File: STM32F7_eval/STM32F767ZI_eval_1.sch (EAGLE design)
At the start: 100 parts, among them CN3 GROVE-4P-CONN-I2C-90D, CN4 GROVE-4P-CONN-AN01-90D, CN5 ARDUINO_COMPAT_IF, CN6 STLINKV21_SWD_IF, CN7 WFT0750CZ09-SMD_, CN8 MCO_IF, CN9 UART_IF, Q1 PMF370XN_, SW1 SKRPACE010_, SW2 SKRPACE010_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

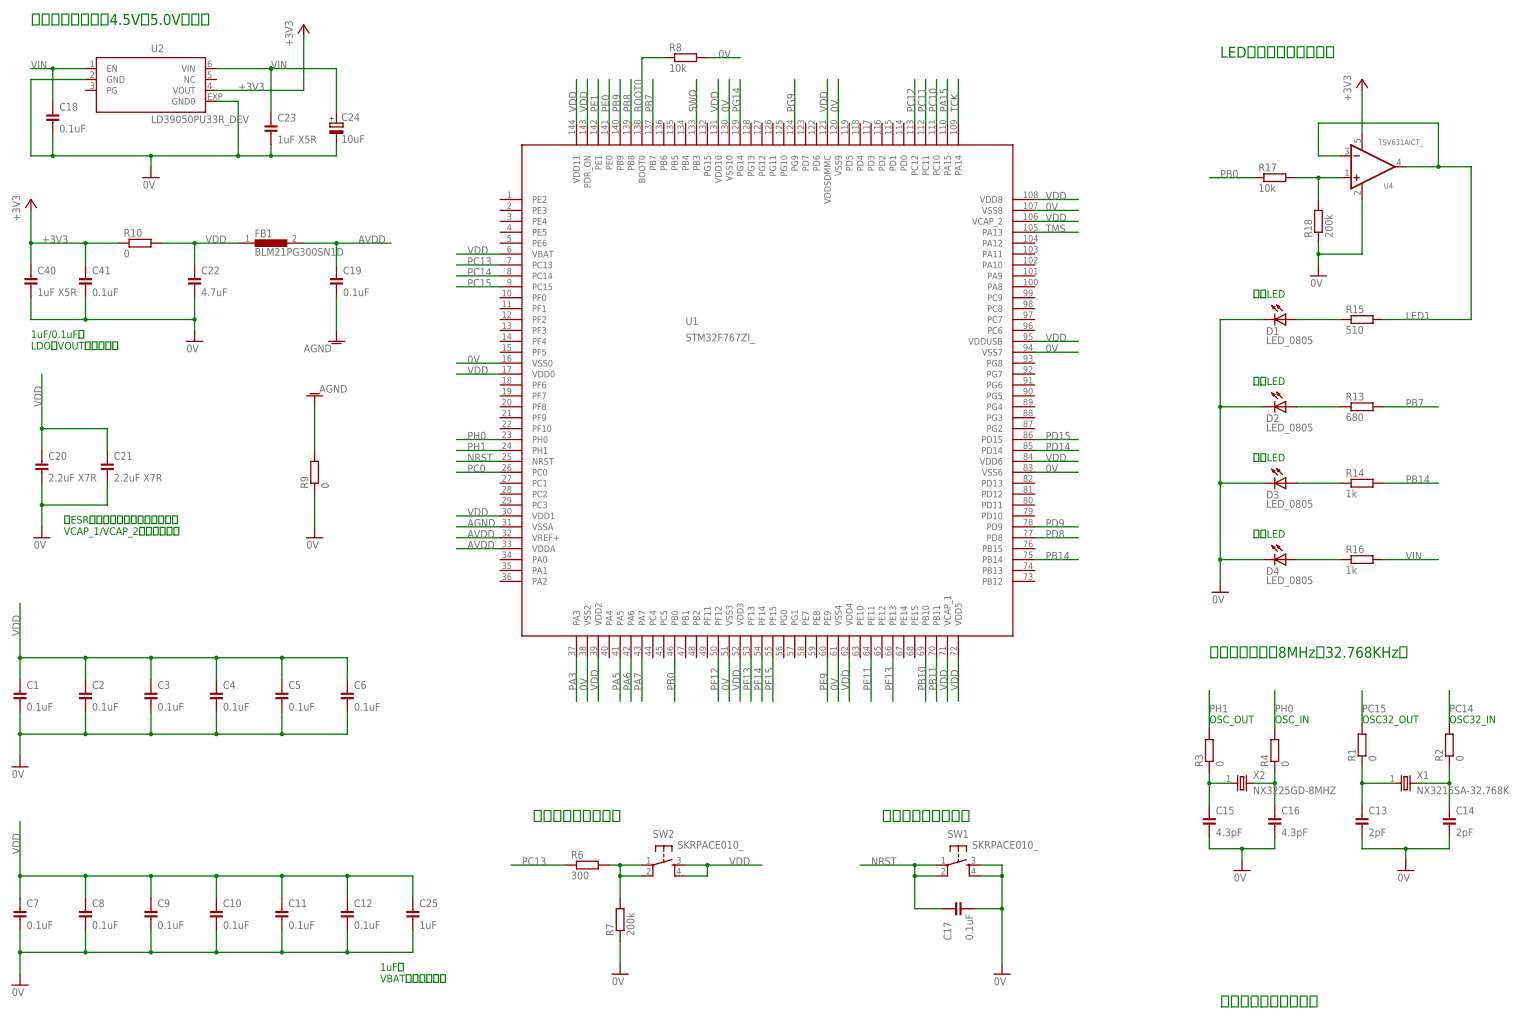
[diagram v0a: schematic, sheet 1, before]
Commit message: 評価回路を修正
・VCAP_1、VCAP_2の配線が間違っていたので修正
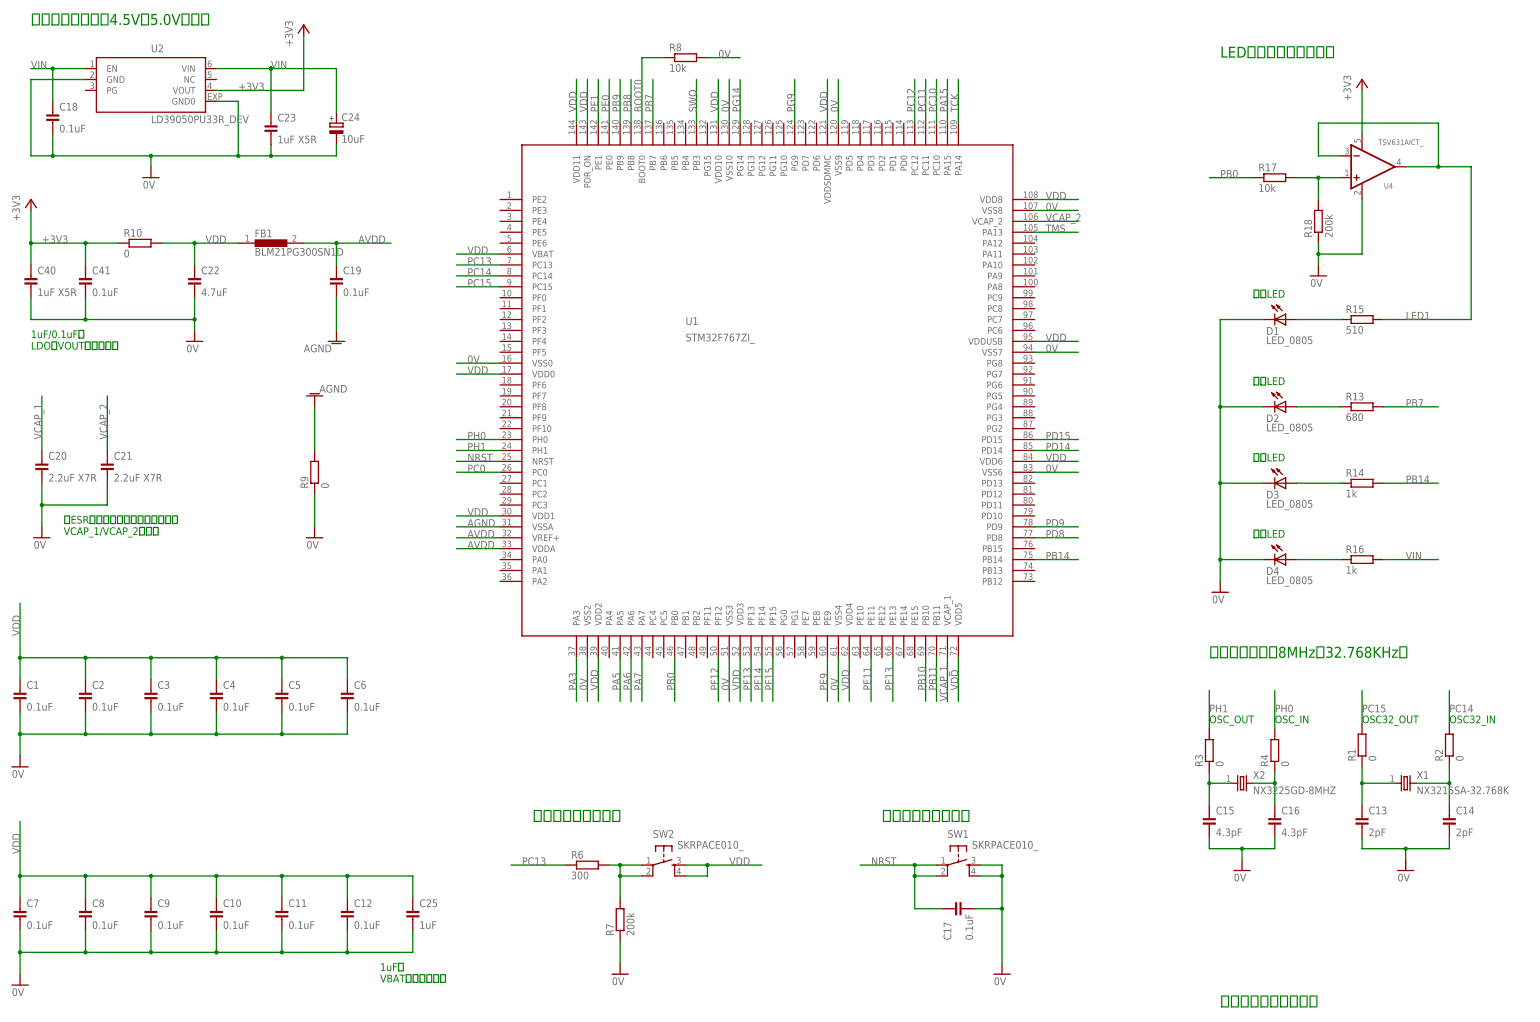
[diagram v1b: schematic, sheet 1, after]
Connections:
- new net VCAP_1: C20.1, U1.VCAP_1
- new net VCAP_2: C21.1, U1.VCAP_2
- net VDD: no longer C20.1, C21.1, U1.VCAP_1, U1.VCAP_2
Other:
- note added: "低ESRのセラミックコンデンサーを VCAP_1/VCAP_2に接続"
- note removed: "低ESRのセラミックコンデンサーを VCAP_1/VCAP_2の近傍に設置"
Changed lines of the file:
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@@
 <text x="218.44" y="55.88" size="2.54" layer="91">リセットボタン回路</text>
 <text x="27.94" y="127" size="1.778" layer="91" align="top-left">低ESRのセラミックコンデンサーを
-VCAP_1/VCAP_2の近傍に設置</text>
+VCAP_1/VCAP_2に接続</text>
 <text x="297.18" y="12.7" size="2.54" layer="91">メインデバイス配線図</text>
 <text x="20.32" y="241.3" size="2.54" layer="91">電源回路（入力は4.5V〜5.0V想定）</text>
@@
 </segment>
 <segment>
-<pinref part="U1" gate="G$1" pin="VCAP_2"/>
-<wire x1="254" y1="195.58" x2="264.16" y2="195.58" width="0.1524" layer="91"/>
-<label x="256.54" y="195.58" size="1.778" layer="95"/>
-</segment>
-<segment>
 <pinref part="U1" gate="G$1" pin="VDDUSB"/>
 <wire x1="254" y1="167.64" x2="264.16" y2="167.64" width="0.1524" layer="91"/>
@@
 <wire x1="236.22" y1="93.98" x2="236.22" y2="83.82" width="0.1524" layer="91"/>
 <label x="236.22" y="86.36" size="1.778" layer="95" rot="R90"/>
-</segment>
-<segment>
-<pinref part="U1" gate="G$1" pin="VCAP_1"/>
-<wire x1="233.68" y1="93.98" x2="233.68" y2="83.82" width="0.1524" layer="91"/>
-<label x="233.68" y="86.36" size="1.778" layer="95" rot="R90"/>
 </segment>
 <segment>
@@
 </segment>
 <segment>
-<pinref part="C20" gate="G$1" pin="1"/>
-<wire x1="22.86" y1="160.02" x2="22.86" y2="147.32" width="0.1524" layer="91"/>
-<pinref part="C21" gate="G$1" pin="1"/>
-<wire x1="22.86" y1="147.32" x2="22.86" y2="142.24" width="0.1524" layer="91"/>
-<wire x1="22.86" y1="147.32" x2="38.1" y2="147.32" width="0.1524" layer="91"/>
-<wire x1="38.1" y1="147.32" x2="38.1" y2="142.24" width="0.1524" layer="91"/>
-<junction x="22.86" y="147.32"/>
-<label x="22.86" y="152.4" size="1.778" layer="95" rot="R90"/>
-</segment>
-<segment>
 <pinref part="SW2" gate="G$1" pin="S"/>
 <wire x1="172.72" y1="45.72" x2="177.8" y2="45.72" width="0.1524" layer="91"/>
@@
 </segment>
 </net>
+<net name="VCAP_2" class="0">
+<segment>
+<pinref part="U1" gate="G$1" pin="VCAP_2"/>
+<wire x1="254" y1="195.58" x2="264.16" y2="195.58" width="0.1524" layer="91"/>
+<label x="256.54" y="195.58" size="1.778" layer="95"/>
+</segment>
+<segment>
+<pinref part="C21" gate="G$1" pin="1"/>
+<wire x1="38.1" y1="142.24" x2="38.1" y2="154.94" width="0.1524" layer="91"/>
+<label x="38.1" y="144.78" size="1.778" layer="95" rot="R90"/>
+</segment>
+</net>
+<net name="VCAP_1" class="0">
+<segment>
+<pinref part="U1" gate="G$1" pin="VCAP_1"/>
+<wire x1="233.68" y1="93.98" x2="233.68" y2="83.82" width="0.1524" layer="91"/>
+<label x="233.68" y="83.82" size="1.778" layer="95" rot="R90"/>
+</segment>
+<segment>
+<pinref part="C20" gate="G$1" pin="1"/>
+<wire x1="22.86" y1="142.24" x2="22.86" y2="154.94" width="0.1524" layer="91"/>
+<label x="22.86" y="144.78" size="1.778" layer="95" rot="R90"/>
+</segment>
+</net>

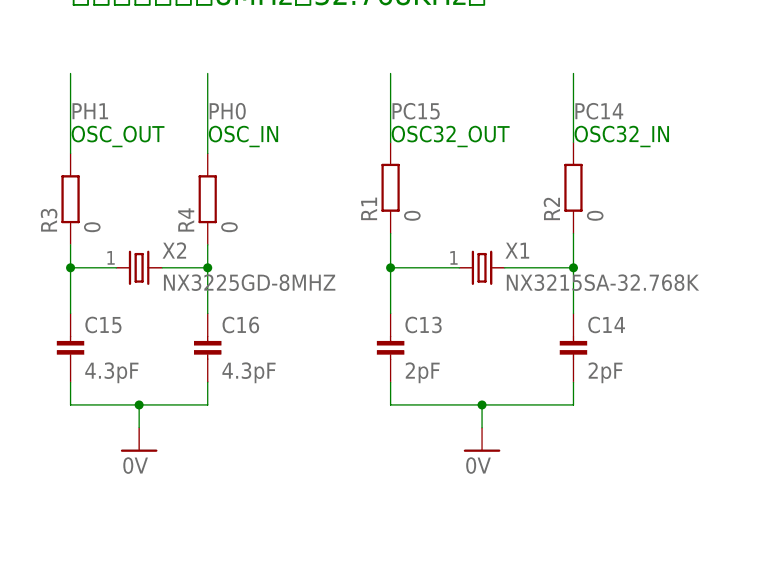
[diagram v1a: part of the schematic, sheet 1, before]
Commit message: 評価回路を修正
・手はんだパターンに修正
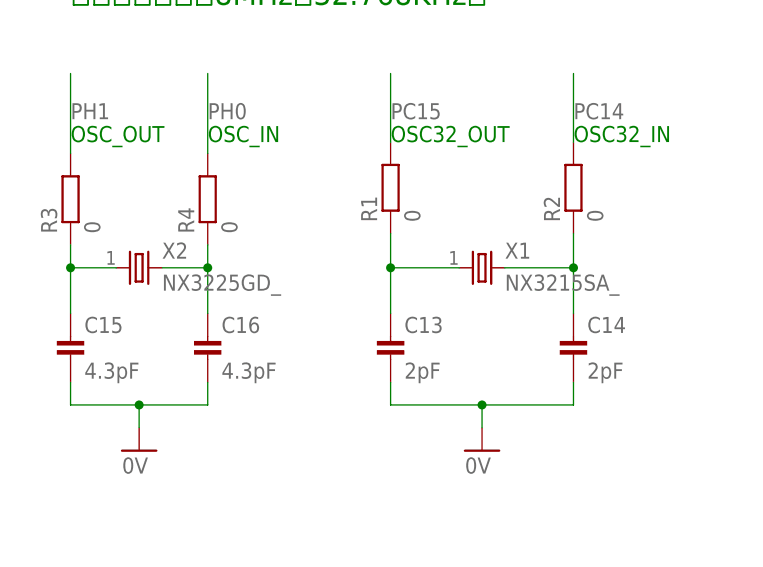
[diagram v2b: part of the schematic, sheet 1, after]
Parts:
- X1: value NX3215SA-32.768K -> NX3215SA_; device Parts:NX3215SA-32.768K -> Parts:NX3215SA_
- X2: value NX3225GD-8MHZ -> NX3225GD_; device Parts:NX3225GD-8MHZ -> Parts:NX3225GD_
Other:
- note added: "フラッシュメモリー回路図"
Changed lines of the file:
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@@
 <setting verticaltext="up"/>
 </settings>
-<grid distance="0.1" unitdist="inch" unit="inch" style="lines" multiple="1" display="yes" altdistance="0.01" altunitdist="inch" altunit="inch"/>
+<grid distance="0.1" unitdist="inch" unit="inch" style="lines" multiple="1" display="no" altdistance="0.01" altunitdist="inch" altunit="inch"/>
 <layers>
 <layer number="1" name="Top" color="4" fill="1" visible="no" active="no"/>
@@
 <part name="C11" library="Parts" deviceset="CAP" device="_0603_DEV" value="0.1uF"/>
 <part name="C12" library="Parts" deviceset="CAP" device="_0603_DEV" value="0.1uF"/>
-<part name="X1" library="Parts" deviceset="NX3215SA" device="-32.768K"/>
+<part name="X1" library="Parts" deviceset="NX3215SA" device="_" value="NX3215SA_"/>
 <part name="C13" library="Parts" deviceset="CAP" device="_0603_DEV" value="2pF"/>
 <part name="C14" library="Parts" deviceset="CAP" device="_0603_DEV" value="2pF"/>
@@
 <part name="R1" library="Parts" deviceset="RESISTOR" device="_0603_DEV" value="0"/>
 <part name="R2" library="Parts" deviceset="RESISTOR" device="_0603_DEV" value="0"/>
-<part name="X2" library="Parts" deviceset="NX3225GD" device="-8MHZ"/>
+<part name="X2" library="Parts" deviceset="NX3225GD" device="_" value="NX3225GD_"/>
 <part name="C15" library="Parts" deviceset="CAP" device="_0603_DEV" value="4.3pF"/>
 <part name="C16" library="Parts" deviceset="CAP" device="_0603_DEV" value="4.3pF"/>
@@
 C1608X5R1A105K
 C3216X7R1C105K </text>
+<text x="104.14" y="160.02" size="2.54" layer="91">フラッシュメモリー回路図</text>
 </plain>
 <instances>

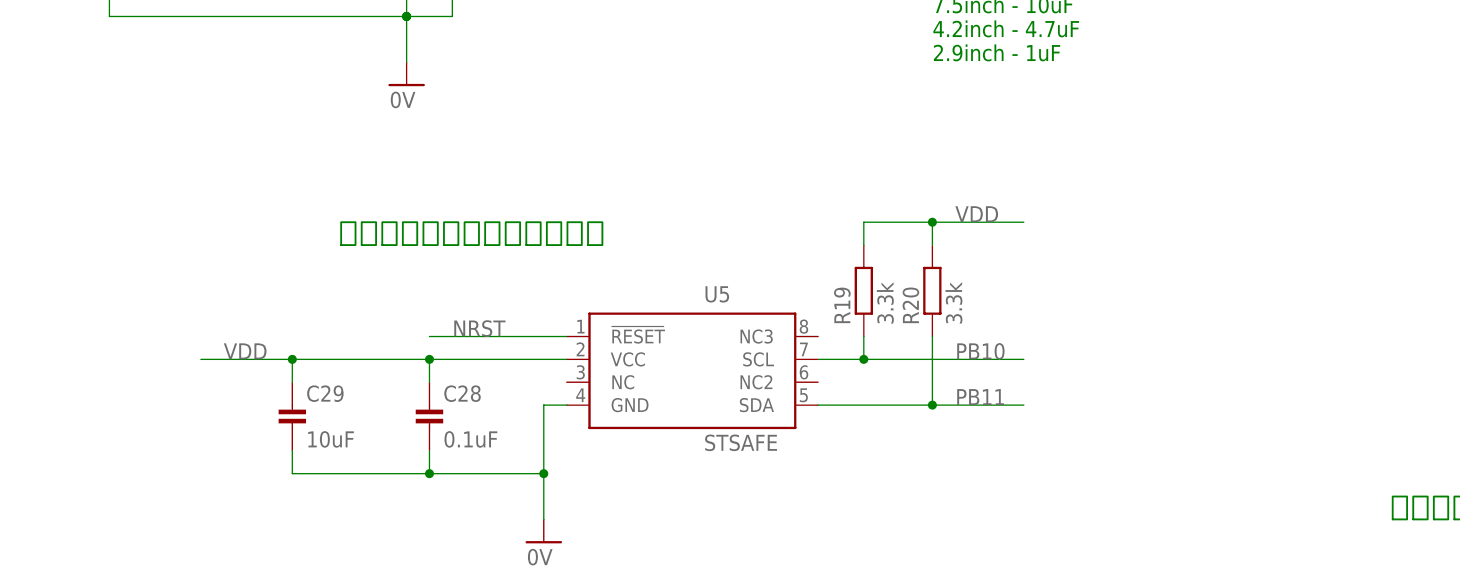
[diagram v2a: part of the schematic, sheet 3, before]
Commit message: 評価回路を修正
・オプションデバイス電圧とメイン電圧間にジャンパーを挿入
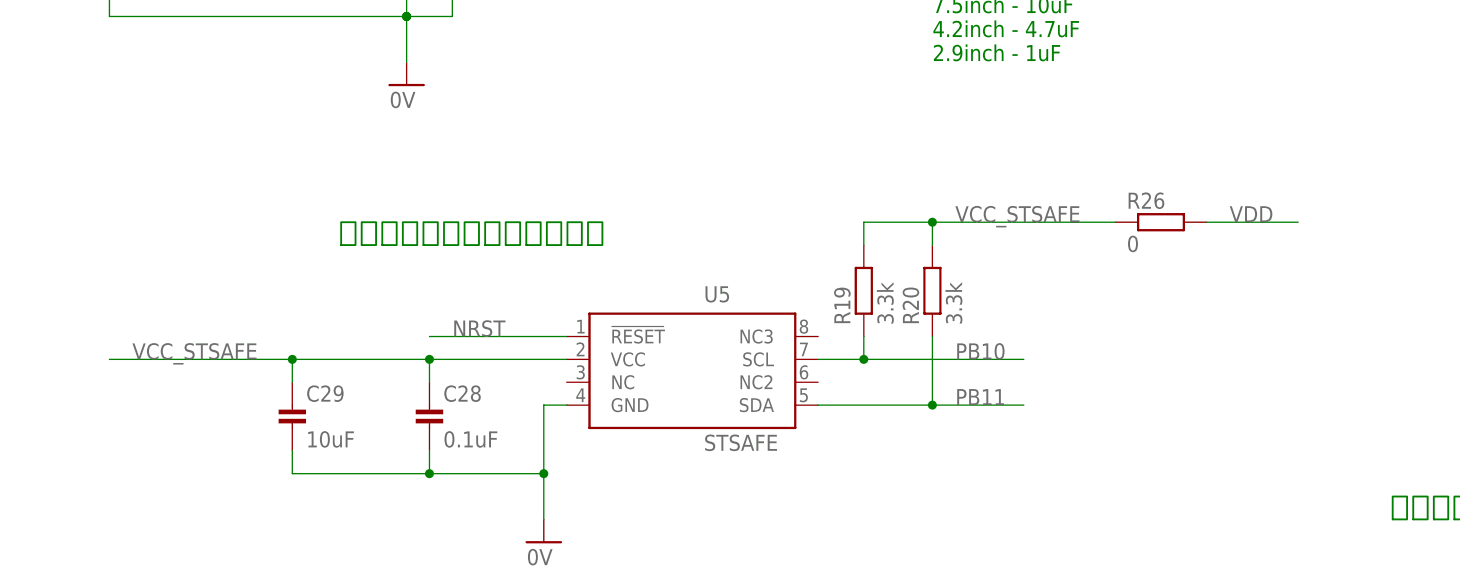
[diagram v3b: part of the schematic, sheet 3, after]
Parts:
- added R26: 0, Parts:RESISTOR_0603_DEV
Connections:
- new net VCC_STSAFE: C28.1, C29.1, R19.2, R20.2, R26.1, U5.VCC
- net VDD: now also R26.2; no longer C28.1, C29.1, R19.2, R20.2, U5.VCC
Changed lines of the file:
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@@
 <part name="R25" library="Parts" deviceset="RESISTOR" device="_0603_DEV" value="0"/>
 <part name="+3V4" library="Supply" deviceset="+3V3" device=""/>
+<part name="R26" library="Parts" deviceset="RESISTOR" device="_0603_DEV" value="0"/>
 </parts>
 <sheets>
@@
 <instance part="R24" gate="G$1" x="154.94" y="114.3"/>
 <instance part="C39" gate="G$1" x="27.94" y="137.16"/>
+<instance part="R26" gate="G$1" x="137.16" y="45.72"/>
 </instances>
 <busses>
@@
 </segment>
 </net>
-<net name="VDD" class="0">
-<segment>
-<pinref part="C29" gate="G$1" pin="1"/>
-<wire x1="76.2" y1="30.48" x2="60.96" y2="30.48" width="0.1524" layer="91"/>
-<wire x1="60.96" y1="30.48" x2="45.72" y2="30.48" width="0.1524" layer="91"/>
-<wire x1="45.72" y1="30.48" x2="45.72" y2="27.94" width="0.1524" layer="91"/>
-<pinref part="C28" gate="G$1" pin="1"/>
-<wire x1="60.96" y1="30.48" x2="60.96" y2="27.94" width="0.1524" layer="91"/>
-<junction x="60.96" y="30.48"/>
-<wire x1="45.72" y1="30.48" x2="35.56" y2="30.48" width="0.1524" layer="91"/>
-<junction x="45.72" y="30.48"/>
-<label x="38.1" y="30.48" size="1.778" layer="95"/>
-<pinref part="U5" gate="G$1" pin="VCC"/>
-</segment>
-<segment>
-<pinref part="R19" gate="G$1" pin="2"/>
-<wire x1="109.22" y1="43.18" x2="109.22" y2="45.72" width="0.1524" layer="91"/>
-<pinref part="R20" gate="G$1" pin="2"/>
-<wire x1="109.22" y1="45.72" x2="116.84" y2="45.72" width="0.1524" layer="91"/>
-<wire x1="116.84" y1="45.72" x2="116.84" y2="43.18" width="0.1524" layer="91"/>
-<wire x1="116.84" y1="45.72" x2="127" y2="45.72" width="0.1524" layer="91"/>
-<junction x="116.84" y="45.72"/>
-<label x="119.38" y="45.72" size="1.778" layer="95"/>
-</segment>
-</net>
 <net name="PB10" class="0">
 <segment>
@@
 </segment>
 </net>
+<net name="VCC_STSAFE" class="0">
+<segment>
+<pinref part="R19" gate="G$1" pin="2"/>
+<wire x1="109.22" y1="43.18" x2="109.22" y2="45.72" width="0.1524" layer="91"/>
+<wire x1="109.22" y1="45.72" x2="116.84" y2="45.72" width="0.1524" layer="91"/>
+<pinref part="R20" gate="G$1" pin="2"/>
+<wire x1="116.84" y1="45.72" x2="137.16" y2="45.72" width="0.1524" layer="91"/>
+<wire x1="116.84" y1="43.18" x2="116.84" y2="45.72" width="0.1524" layer="91"/>
+<junction x="116.84" y="45.72"/>
+<label x="119.38" y="45.72" size="1.778" layer="95"/>
+<pinref part="R26" gate="G$1" pin="1"/>
+</segment>
+<segment>
+<pinref part="U5" gate="G$1" pin="VCC"/>
+<wire x1="76.2" y1="30.48" x2="60.96" y2="30.48" width="0.1524" layer="91"/>
+<pinref part="C29" gate="G$1" pin="1"/>
+<wire x1="60.96" y1="30.48" x2="45.72" y2="30.48" width="0.1524" layer="91"/>
+<wire x1="45.72" y1="30.48" x2="25.4" y2="30.48" width="0.1524" layer="91"/>
+<wire x1="45.72" y1="27.94" x2="45.72" y2="30.48" width="0.1524" layer="91"/>
+<junction x="45.72" y="30.48"/>
+<pinref part="C28" gate="G$1" pin="1"/>
+<wire x1="60.96" y1="27.94" x2="60.96" y2="30.48" width="0.1524" layer="91"/>
+<junction x="60.96" y="30.48"/>
+<label x="27.94" y="30.48" size="1.778" layer="95"/>
+</segment>
+</net>
+<net name="VDD" class="0">
+<segment>
+<pinref part="R26" gate="G$1" pin="2"/>
+<wire x1="147.32" y1="45.72" x2="157.48" y2="45.72" width="0.1524" layer="91"/>
+<label x="149.86" y="45.72" size="1.778" layer="95"/>
+</segment>
+</net>
